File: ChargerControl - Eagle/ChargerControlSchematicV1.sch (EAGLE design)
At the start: 30 parts, among them T1 2N2222, T2 2N2222, T3 2N2222

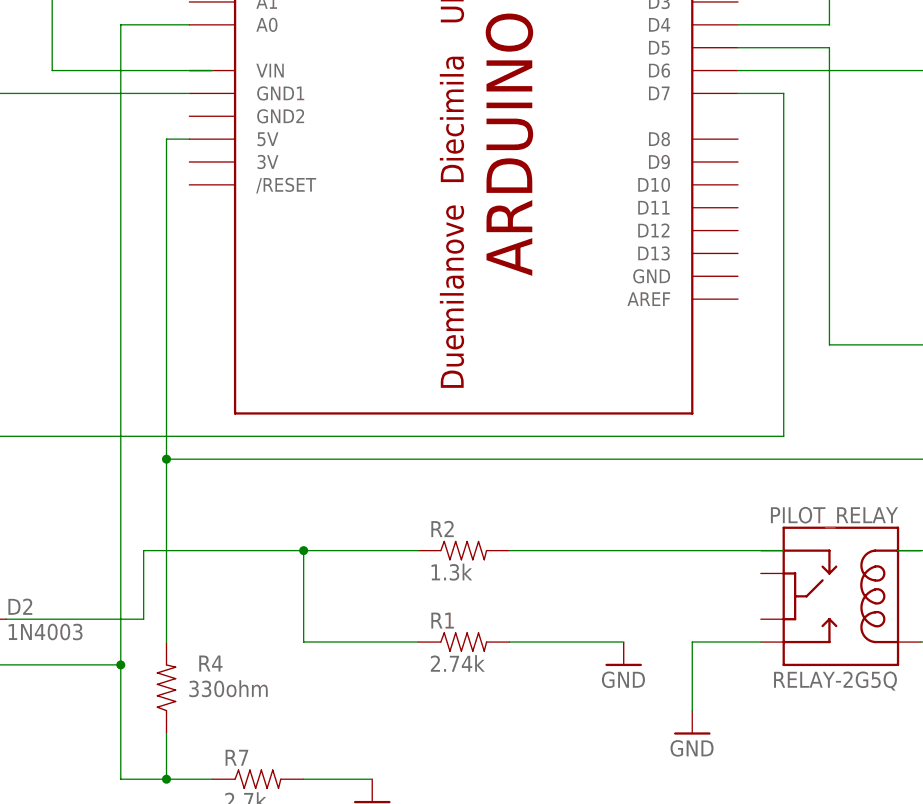
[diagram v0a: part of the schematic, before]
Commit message: Show time option added. Fixed the prix test to be "smarter". Use a 5v out signal for the prox test so it isn't always "hot" which was messing up my home EVSE
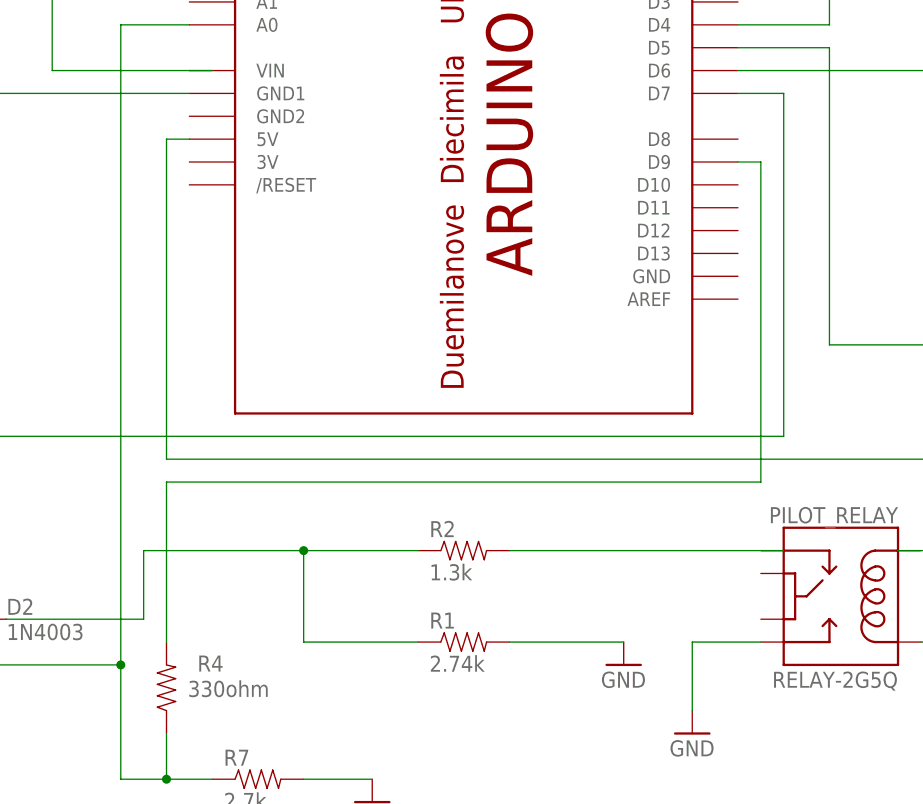
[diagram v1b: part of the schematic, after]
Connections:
- new net N$18: R4.2, U$2.D9
- net N$10: no longer R4.2
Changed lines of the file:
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@@
 <wire x1="60.96" y1="93.98" x2="58.42" y2="93.98" width="0.1524" layer="91"/>
 <wire x1="58.42" y1="93.98" x2="58.42" y2="58.42" width="0.1524" layer="91"/>
-<pinref part="R4" gate="G$1" pin="2"/>
-<wire x1="58.42" y1="58.42" x2="58.42" y2="38.1" width="0.1524" layer="91"/>
 <wire x1="58.42" y1="58.42" x2="162.56" y2="58.42" width="0.1524" layer="91"/>
 <pinref part="R11" gate="G$1" pin="1"/>
 <wire x1="162.56" y1="58.42" x2="162.56" y2="76.2" width="0.1524" layer="91"/>
-<junction x="58.42" y="58.42"/>
 </segment>
 </net>
@@
 </segment>
 </net>
+<net name="N$18" class="0">
+<segment>
+<pinref part="R4" gate="G$1" pin="2"/>
+<pinref part="U$2" gate="G$1" pin="D9"/>
+<wire x1="121.92" y1="91.44" x2="124.46" y2="91.44" width="0.1524" layer="91"/>
+<wire x1="124.46" y1="91.44" x2="124.46" y2="55.88" width="0.1524" layer="91"/>
+<wire x1="124.46" y1="55.88" x2="58.42" y2="55.88" width="0.1524" layer="91"/>
+<wire x1="58.42" y1="55.88" x2="58.42" y2="38.1" width="0.1524" layer="91"/>
+</segment>
+</net>
